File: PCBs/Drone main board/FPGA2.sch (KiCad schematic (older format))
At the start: 1 part, among them U1201 10CL040_F484

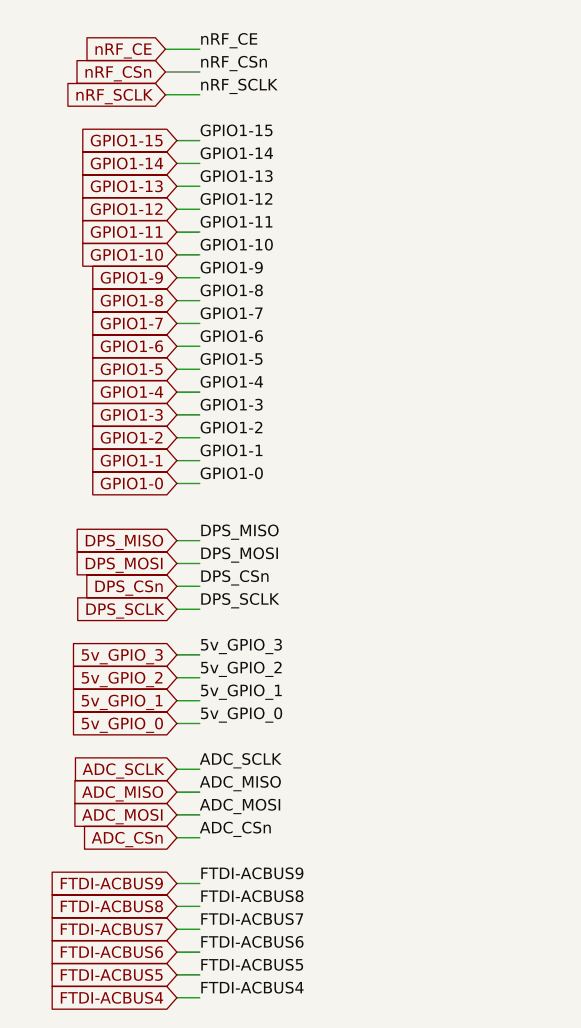
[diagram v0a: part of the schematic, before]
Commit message: Finished (?) the schematic check and update. Next: PCB update
Signed-off-by: Eldalote.Electronics <Eldalote.Electronics@gmail.com>
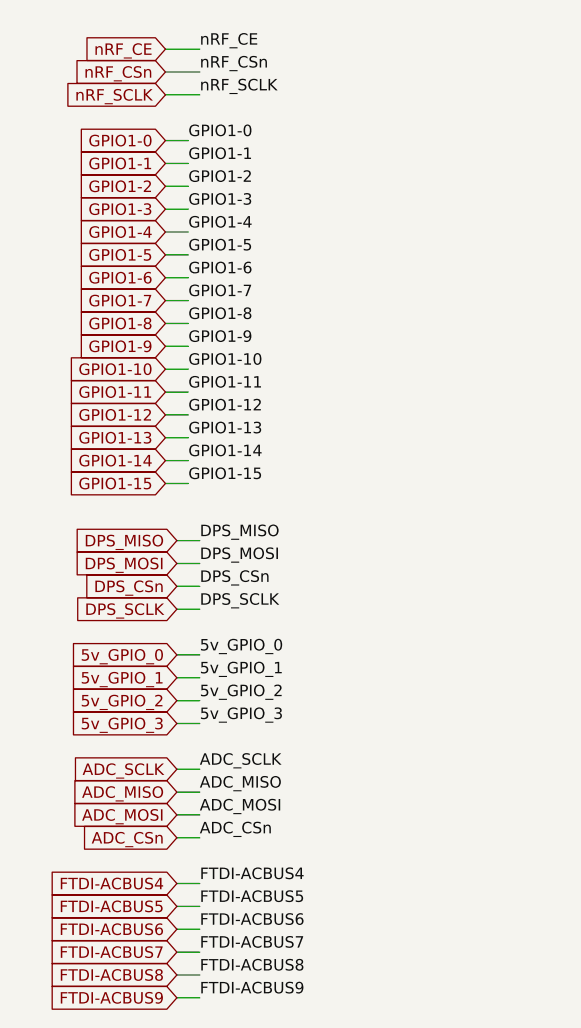
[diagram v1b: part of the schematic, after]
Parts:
- U1201: MfNr (none) -> 10CL040Y
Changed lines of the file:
@@
 F 4 "TRUE" H 6400 -5415 35  0001 L CNN "SPLIT_INST"
 F 5 "(S1+S2+S3+S4+S5+S6+S7+S8+S9+S10+S11+S12+S13)" H 6400 -5460 35  0001 L CNN "SWAP_INFO"
+F 6 "10CL040Y" H 5350 600 50  0001 C CNN "MfNr"
 	5    5350 600
 	1    0    0    -1
@@
 F 4 "TRUE" H 9300 -5415 35  0001 L CNN "SPLIT_INST"
 F 5 "(S1+S2+S3+S4+S5+S6+S7+S8+S9+S10+S11+S12+S13)" H 9300 -5460 35  0001 L CNN "SWAP_INFO"
+F 6 "10CL040Y" H 8250 600 50  0001 C CNN "MfNr"
 	6    8250 600
 	1    0    0    -1
@@
 F 4 "TRUE" H 11550 -5365 35  0001 L CNN "SPLIT_INST"
 F 5 "(S1+S2+S3+S4+S5+S6+S7+S8+S9+S10+S11+S12+S13)" H 11550 -5410 35  0001 L CNN "SWAP_INFO"
+F 6 "10CL040Y" H 10500 650 50  0001 C CNN "MfNr"
 	7    10500 650
 	1    0    0    -1
@@
 nRF_SCLK
 Wire Wire Line
-	1550 2550 1650 2550
-Wire Wire Line
-	1550 2350 1650 2350
-Wire Wire Line
-	1550 2150 1650 2150
-Wire Wire Line
-	1550 1950 1650 1950
-Wire Wire Line
-	1550 1750 1650 1750
-Wire Wire Line
-	1550 1550 1650 1550
-Wire Wire Line
-	1550 1350 1650 1350
-Wire Wire Line
-	1550 1150 1650 1150
-Text Label 1650 2550 0    50   ~ 0
+	1500 1050 1600 1050
+Wire Wire Line
+	1500 1250 1600 1250
+Wire Wire Line
+	1500 1450 1600 1450
+Wire Wire Line
+	1500 1650 1600 1650
+Wire Wire Line
+	1500 1850 1600 1850
+Wire Wire Line
+	1500 2050 1600 2050
+Wire Wire Line
+	1500 2250 1600 2250
+Wire Wire Line
+	1500 2450 1600 2450
+Text Label 1600 1050 0    50   ~ 0
 GPIO1-0
-Text Label 1650 2350 0    50   ~ 0
+Text Label 1600 1250 0    50   ~ 0
 GPIO1-2
-Text Label 1650 2150 0    50   ~ 0
+Text Label 1600 1450 0    50   ~ 0
 GPIO1-4
-Text Label 1650 1950 0    50   ~ 0
+Text Label 1600 1650 0    50   ~ 0
 GPIO1-6
-Text Label 1650 1750 0    50   ~ 0
+Text Label 1600 1850 0    50   ~ 0
 GPIO1-8
-Text Label 1650 1550 0    50   ~ 0
+Text Label 1600 2050 0    50   ~ 0
 GPIO1-10
-Text Label 1650 1350 0    50   ~ 0
+Text Label 1600 2250 0    50   ~ 0
 GPIO1-12
-Text Label 1650 1150 0    50   ~ 0
+Text Label 1600 2450 0    50   ~ 0
 GPIO1-14
 Wire Wire Line
-	1550 2450 1650 2450
-Wire Wire Line
-	1550 2250 1650 2250
-Wire Wire Line
-	1550 2050 1650 2050
-Wire Wire Line
-	1550 1850 1650 1850
-Wire Wire Line
-	1550 1650 1650 1650
-Wire Wire Line
-	1550 1450 1650 1450
-Wire Wire Line
-	1550 1250 1650 1250
-Wire Wire Line
-	1550 1050 1650 1050
-Text Label 1650 2450 0    50   ~ 0
+	1500 1150 1600 1150
+Wire Wire Line
+	1500 1350 1600 1350
+Wire Wire Line
+	1500 1550 1600 1550
+Wire Wire Line
+	1500 1750 1600 1750
+Wire Wire Line
+	1500 1950 1600 1950
+Wire Wire Line
+	1500 2150 1600 2150
+Wire Wire Line
+	1500 2350 1600 2350
+Wire Wire Line
+	1500 2550 1600 2550
+Text Label 1600 1150 0    50   ~ 0
 GPIO1-1
-Text Label 1650 2250 0    50   ~ 0
+Text Label 1600 1350 0    50   ~ 0
 GPIO1-3
-Text Label 1650 2050 0    50   ~ 0
+Text Label 1600 1550 0    50   ~ 0
 GPIO1-5
-Text Label 1650 1850 0    50   ~ 0
+Text Label 1600 1750 0    50   ~ 0
 GPIO1-7
-Text Label 1650 1650 0    50   ~ 0
+Text Label 1600 1950 0    50   ~ 0
 GPIO1-9
-Text Label 1650 1450 0    50   ~ 0
+Text Label 1600 2150 0    50   ~ 0
 GPIO1-11
-Text Label 1650 1250 0    50   ~ 0
+Text Label 1600 2350 0    50   ~ 0
 GPIO1-13
-Text Label 1650 1050 0    50   ~ 0
+Text Label 1600 2550 0    50   ~ 0
 GPIO1-15
-Text GLabel 1550 2550 0    50   Input ~ 0
+Text GLabel 1500 1050 0    50   Input ~ 0
 GPIO1-0
-Text GLabel 1550 2450 0    50   Input ~ 0
+Text GLabel 1500 1150 0    50   Input ~ 0
 GPIO1-1
-Text GLabel 1550 2350 0    50   Input ~ 0
+Text GLabel 1500 1250 0    50   Input ~ 0
 GPIO1-2
-Text GLabel 1550 2250 0    50   Input ~ 0
+Text GLabel 1500 1350 0    50   Input ~ 0
 GPIO1-3
-Text GLabel 1550 2150 0    50   Input ~ 0
+Text GLabel 1500 1450 0    50   Input ~ 0
 GPIO1-4
-Text GLabel 1550 2050 0    50   Input ~ 0
+Text GLabel 1500 1550 0    50   Input ~ 0
 GPIO1-5
-Text GLabel 1550 1950 0    50   Input ~ 0
+Text GLabel 1500 1650 0    50   Input ~ 0
 GPIO1-6
-Text GLabel 1550 1850 0    50   Input ~ 0
+Text GLabel 1500 1750 0    50   Input ~ 0
 GPIO1-7
-Text GLabel 1550 1750 0    50   Input ~ 0
+Text GLabel 1500 1850 0    50   Input ~ 0
 GPIO1-8
-Text GLabel 1550 1650 0    50   Input ~ 0
+Text GLabel 1500 1950 0    50   Input ~ 0
 GPIO1-9
-Text GLabel 1550 1550 0    50   Input ~ 0
+Text GLabel 1500 2050 0    50   Input ~ 0
 GPIO1-10
-Text GLabel 1550 1450 0    50   Input ~ 0
+Text GLabel 1500 2150 0    50   Input ~ 0
 GPIO1-11
-Text GLabel 1550 1350 0    50   Input ~ 0
+Text GLabel 1500 2250 0    50   Input ~ 0
 GPIO1-12
-Text GLabel 1550 1250 0    50   Input ~ 0
+Text GLabel 1500 2350 0    50   Input ~ 0
 GPIO1-13
-Text GLabel 1550 1150 0    50   Input ~ 0
+Text GLabel 1500 2450 0    50   Input ~ 0
 GPIO1-14
-Text GLabel 1550 1050 0    50   Input ~ 0
+Text GLabel 1500 2550 0    50   Input ~ 0
 GPIO1-15
 Wire Wire Line
@@
 Text Label 7950 1250 2    50   ~ 0
 DPS_MISO
+Text GLabel 1550 3300 0    50   Input ~ 0
+5v_GPIO_0
+Text GLabel 1550 3400 0    50   Input ~ 0
+5v_GPIO_1
+Text GLabel 1550 3500 0    50   Input ~ 0
+5v_GPIO_2
 Text GLabel 1550 3600 0    50   Input ~ 0
-5v_GPIO_0
-Text GLabel 1550 3500 0    50   Input ~ 0
+5v_GPIO_3
+Wire Wire Line
+	1550 3600 1650 3600
+Wire Wire Line
+	1550 3500 1650 3500
+Wire Wire Line
+	1550 3400 1650 3400
+Wire Wire Line
+	1550 3300 1650 3300
+Text Label 1650 3600 0    50   ~ 0
+5v_GPIO_3
+Text Label 1650 3500 0    50   ~ 0
+5v_GPIO_2
+Text Label 1650 3400 0    50   ~ 0
 5v_GPIO_1
-Text GLabel 1550 3400 0    50   Input ~ 0
-5v_GPIO_2
-Text GLabel 1550 3300 0    50   Input ~ 0
-5v_GPIO_3
-Wire Wire Line
-	1550 3300 1650 3300
-Wire Wire Line
-	1550 3400 1650 3400
-Wire Wire Line
-	1550 3500 1650 3500
-Wire Wire Line
-	1550 3600 1650 3600
 Text Label 1650 3300 0    50   ~ 0
-5v_GPIO_3
-Text Label 1650 3400 0    50   ~ 0
-5v_GPIO_2
-Text Label 1650 3500 0    50   ~ 0
-5v_GPIO_1
-Text Label 1650 3600 0    50   ~ 0
 5v_GPIO_0
 Wire Wire Line
@@
 Text Label 5050 1550 2    50   ~ 0
 ADC_SCLK
+Text Label 1650 4300 0    50   ~ 0
+FTDI-ACBUS4
+Text Label 1650 4400 0    50   ~ 0
+FTDI-ACBUS5
+Text Label 1650 4500 0    50   ~ 0
+FTDI-ACBUS6
+Text Label 1650 4600 0    50   ~ 0
+FTDI-ACBUS7
+Wire Wire Line
+	1650 4300 1550 4300
+Wire Wire Line
+	1650 4400 1550 4400
+Wire Wire Line
+	1650 4500 1550 4500
+Wire Wire Line
+	1650 4600 1550 4600
+Text GLabel 1550 4300 0    50   Input ~ 0
+FTDI-ACBUS4
+Text GLabel 1550 4400 0    50   Input ~ 0
+FTDI-ACBUS5
+Text GLabel 1550 4500 0    50   Input ~ 0
+FTDI-ACBUS6
+Text GLabel 1550 4600 0    50   Input ~ 0
+FTDI-ACBUS7
+Text Label 1650 4700 0    50   ~ 0
+FTDI-ACBUS8
 Text Label 1650 4800 0    50   ~ 0
-FTDI-ACBUS4
-Text Label 1650 4700 0    50   ~ 0
-FTDI-ACBUS5
-Text Label 1650 4600 0    50   ~ 0
-FTDI-ACBUS6
-Text Label 1650 4500 0    50   ~ 0
-FTDI-ACBUS7
+FTDI-ACBUS9
+Wire Wire Line
+	1650 4700 1550 4700
 Wire Wire Line
 	1650 4800 1550 4800
-Wire Wire Line
-	1650 4700 1550 4700
-Wire Wire Line
-	1650 4600 1550 4600
-Wire Wire Line
-	1650 4500 1550 4500
+Text GLabel 1550 4700 0    50   Input ~ 0
+FTDI-ACBUS8
 Text GLabel 1550 4800 0    50   Input ~ 0
-FTDI-ACBUS4
-Text GLabel 1550 4700 0    50   Input ~ 0
-FTDI-ACBUS5
-Text GLabel 1550 4600 0    50   Input ~ 0
-FTDI-ACBUS6
-Text GLabel 1550 4500 0    50   Input ~ 0
-FTDI-ACBUS7
-Text Label 1650 4400 0    50   ~ 0
-FTDI-ACBUS8
-Text Label 1650 4300 0    50   ~ 0
-FTDI-ACBUS9
-Wire Wire Line
-	1650 4400 1550 4400
-Wire Wire Line
-	1650 4300 1550 4300
-Text GLabel 1550 4400 0    50   Input ~ 0
-FTDI-ACBUS8
-Text GLabel 1550 4300 0    50   Input ~ 0
 FTDI-ACBUS9
 Text Label 5050 650  2    50   ~ 0
